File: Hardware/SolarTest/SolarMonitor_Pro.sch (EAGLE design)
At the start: 29 parts, among them J6 5.5x2.1mm Barrel, J8 CONN_42.54_SCREW

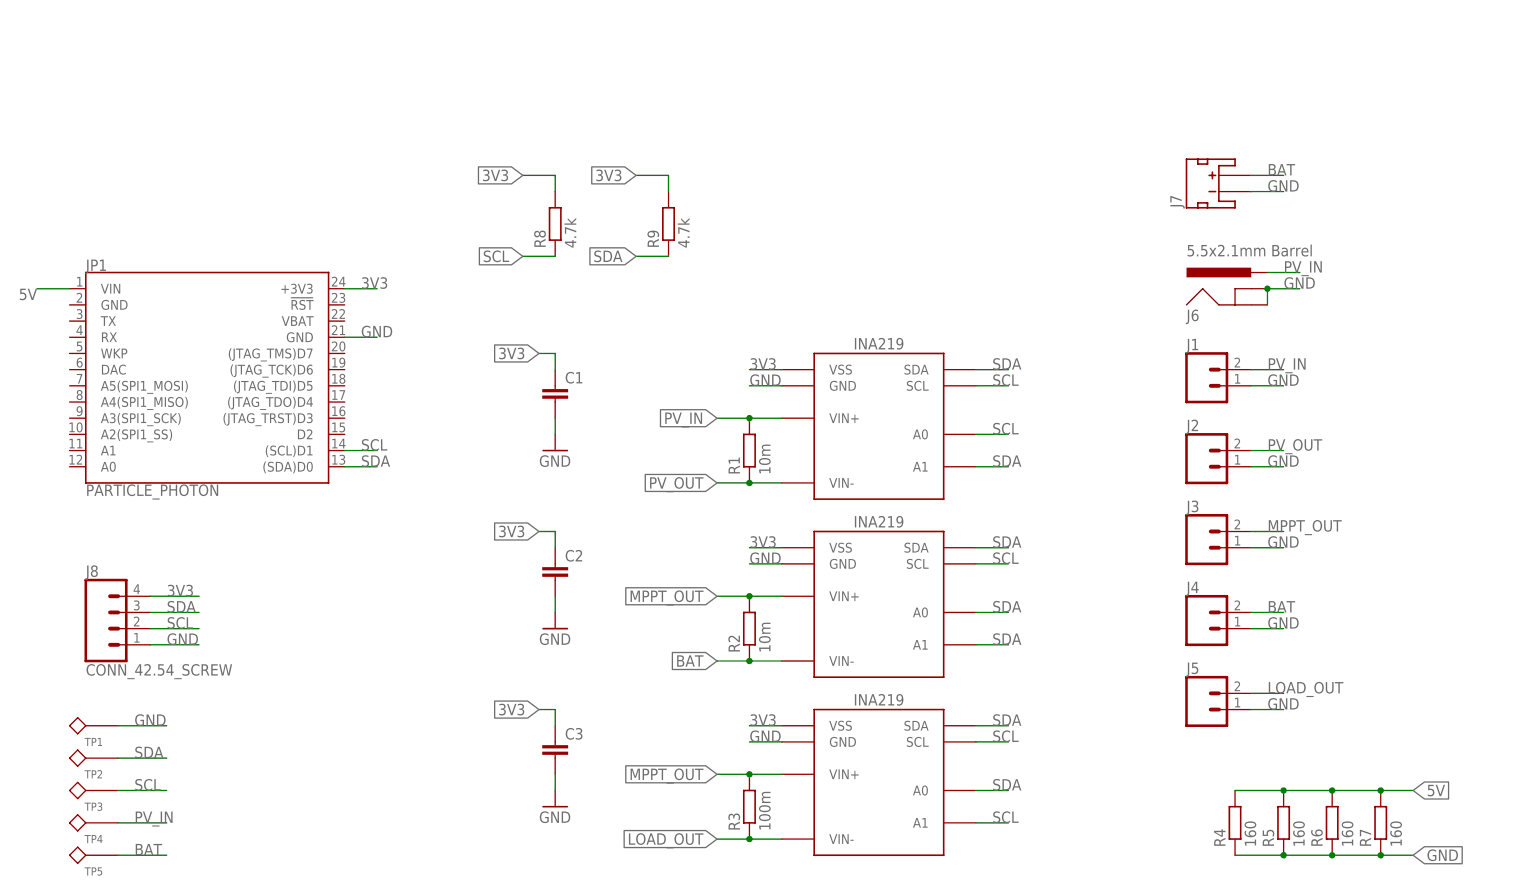
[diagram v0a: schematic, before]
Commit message: Updated solar monitor board, v0 ready for fab
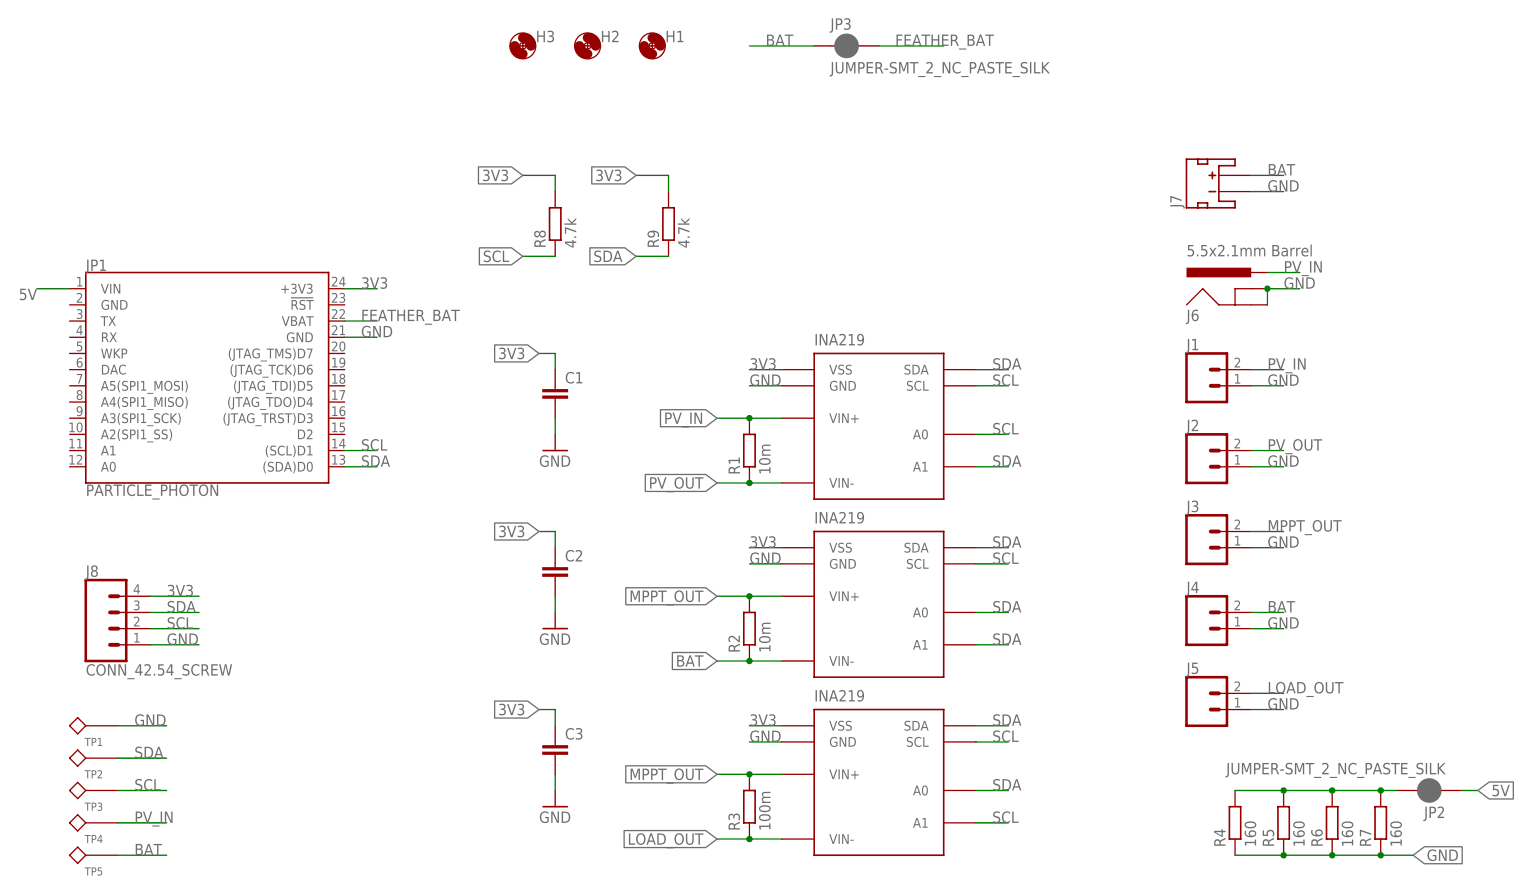
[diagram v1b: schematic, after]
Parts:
- removed U$2, U$3, U$4: INA219DCN, bschulz:INA219DCN
- added H1, H2, H3: (no value), bschulz:MOUNTING_HOLE4_NP
- added JP2, JP3: JUMPER-SMT_2_NC_PASTE_SILK, SparkFun-Jumpers:JUMPER-SMT_2_NC_PASTE_SILK
- added U1, U2, U3: INA219DCN, bschulz:INA219DCN
- C1, C2, C3: device bschulz:C-EUC0402 -> bschulz_passives:C-EU0.1UFC0402
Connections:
- new net FEATHER_BAT: JP1.VBAT, JP3.2
- new net LOAD: JP2.2, R4.2, R5.2, R6.2, R7.2
- net 3V3: now also U1.VSS, U2.VSS, U3.VSS; no longer U$2.VSS, U$3.VSS, U$4.VSS
- net 5V: now also JP2.1; no longer R4.2, R5.2, R6.2, R7.2
- net BAT: now also JP3.1, U2.VIN-; no longer U$3.VIN-
- net GND: now also U1.GND, U2.GND, U3.GND; no longer U$2.GND, U$3.GND, U$4.GND
- net LOAD_OUT: now also U3.VIN-; no longer U$4.VIN-
- net MPPT_OUT: now also U2.VIN+, U3.VIN+; no longer U$3.VIN+, U$4.VIN+
- net PV_IN: now also U1.VIN+; no longer U$2.VIN+
- net PV_OUT: now also U1.VIN-; no longer U$2.VIN-
- net SCL: now also U1.A0, U1.SCL, U2.SCL, U3.A1, U3.SCL; no longer U$2.A0, U$2.SCL, U$3.SCL, U$4.A1, U$4.SCL
- net SDA: now also U1.A1, U1.SDA, U2.A0, U2.A1, U2.SDA, U3.A0, U3.SDA; no longer U$2.A1, U$2.SDA, U$3.A0, U$3.A1, U$3.SDA, U$4.A0, U$4.SDA
